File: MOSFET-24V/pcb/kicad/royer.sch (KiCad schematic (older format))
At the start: 26 parts, among them J1 9-24V, J2 COIL, Q1 IRFB4410, Q2 IRFD110, Q3 IRFD110, Q4 IRFB4410

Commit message: compacting PCB
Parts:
- removed C5: 4.7uF, Capacitors_Tantalum_SMD:Tantalum_Case-C_EIA-6032-28_Hand, symbol CP
- added C5: 47nF, Capacitors_SMD:C_1206_HandSoldering, symbol C
- added R6: 1k, Resistors_SMD:R_1206_HandSoldering, symbol R
- R5: renamed from R7; value 1.5k -> 1k
- renumbered R3 to R2, R4 to R3, R5 to R4
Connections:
- net 24V: now also R6.1; no longer R5.1
- net 9V: now also C5.1
- net GND: now also C5.2
- new net: R5.1, R6.2
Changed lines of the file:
@@
 $EndComp
 $Comp
-L R R3
+L R R2
 U 1 1 584180F8
 P 3250 4300
-F 0 "R3" V 3330 4300 50  0000 C CNN
+F 0 "R2" V 3330 4300 50  0000 C CNN
 F 1 "47k" V 3250 4300 50  0000 C CNN
 F 2 "Resistors_SMD:R_1206_HandSoldering" V 3180 4300 50  0001 C CNN
@@
 $EndComp
 $Comp
-L R R5
+L R R4
 U 1 1 58419AC4
 P 3800 4950
-F 0 "R5" V 3880 4950 50  0000 C CNN
+F 0 "R4" V 3880 4950 50  0000 C CNN
 F 1 "33k" V 3800 4950 50  0000 C CNN
 F 2 "Resistors_SMD:R_1206_HandSoldering" V 3730 4950 50  0001 C CNN
@@
 $EndComp
 $Comp
-L R R4
+L R R3
 U 1 1 58419ACA
 P 3550 4300
-F 0 "R4" V 3630 4300 50  0000 C CNN
+F 0 "R3" V 3630 4300 50  0000 C CNN
 F 1 "47k" V 3550 4300 50  0000 C CNN
 F 2 "Resistors_SMD:R_1206_HandSoldering" V 3480 4300 50  0001 C CNN
@@
 Connection ~ 4800 4650
 $Comp
-L R R7
+L R R5
 U 1 1 5841F0FF
 P 5100 4350
-F 0 "R7" V 5180 4350 50  0000 C CNN
-F 1 "1.5k" V 5100 4350 50  0000 C CNN
+F 0 "R5" V 5180 4350 50  0000 C CNN
+F 1 "1k" V 5100 4350 50  0000 C CNN
 F 2 "Resistors_SMD:R_1206_HandSoldering" V 5030 4350 50  0001 C CNN
 F 3 "" H 5100 4350 50  0000 C CNN
@@
 Connection ~ 3800 4100
 Connection ~ 4450 5800
-Wire Wire Line
-	5100 3350 5100 4200
 Wire Wire Line
 	3400 3700 5100 3700
@@
 Connection ~ 2350 3850
 $Comp
-L CP C5
-U 1 1 58F49BFC
+L C C5
+U 1 1 58F49D26
 P 4800 4900
 F 0 "C5" H 4825 5000 50  0000 L CNN
-F 1 "4.7uF" H 4825 4800 50  0000 L CNN
-F 2 "Capacitors_Tantalum_SMD:Tantalum_Case-C_EIA-6032-28_Hand" H 4838 4750 50  0001 C CNN
+F 1 "47nF" H 4825 4800 50  0000 L CNN
+F 2 "Capacitors_SMD:C_1206_HandSoldering" H 4838 4750 50  0001 C CNN
 F 3 "" H 4800 4900 50  0000 C CNN
 	1    4800 4900
 	1    0    0    -1
 $EndComp
+$Comp
+L R R6
+U 1 1 58F4A65C
+P 5100 4050
+F 0 "R6" V 5180 4050 50  0000 C CNN
+F 1 "1k" V 5100 4050 50  0000 C CNN
+F 2 "Resistors_SMD:R_1206_HandSoldering" V 5030 4050 50  0001 C CNN
+F 3 "" H 5100 4050 50  0000 C CNN
+	1    5100 4050
+	1    0    0    -1
+$EndComp
+Wire Wire Line
+	5100 3350 5100 3900
 $EndSCHEMATC

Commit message: enlarging holes 3.2->3.5 mm# Please enter the commit message for your changes. Lines starting
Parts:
- H1, H2, H3, H4: value 3.2mm -> 3.5mm; footprint Mounting_Holes:MountingHole_3.2mm_M3_ISO14580_Pad -> Mounting_Holes:MountingHole_3.5mm_Pad
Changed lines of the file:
@@
 P 3250 6200
 F 0 "H2" H 3250 6300 50  0000 C CNN
-F 1 "3.2mm" V 3350 6200 50  0000 C CNN
-F 2 "Mounting_Holes:MountingHole_3.2mm_M3_ISO14580_Pad" H 3250 6200 50  0001 C CNN
+F 1 "3.5mm" V 3350 6200 50  0000 C CNN
+F 2 "Mounting_Holes:MountingHole_3.5mm_Pad" H 3250 6200 50  0001 C CNN
 F 3 "" H 3250 6200 50  0000 C CNN
 	1    3250 6200
@@
 P 2900 6200
 F 0 "H1" H 2900 6300 50  0000 C CNN
-F 1 "3.2mm" V 3000 6200 50  0000 C CNN
-F 2 "Mounting_Holes:MountingHole_3.2mm_M3_ISO14580_Pad" H 2900 6200 50  0001 C CNN
+F 1 "3.5mm" V 3000 6200 50  0000 C CNN
+F 2 "Mounting_Holes:MountingHole_3.5mm_Pad" H 2900 6200 50  0001 C CNN
 F 3 "" H 2900 6200 50  0000 C CNN
 	1    2900 6200
@@
 P 3900 6200
 F 0 "H4" H 3900 6300 50  0000 C CNN
-F 1 "3.2mm" V 4000 6200 50  0000 C CNN
-F 2 "Mounting_Holes:MountingHole_3.2mm_M3_ISO14580_Pad" H 3900 6200 50  0001 C CNN
+F 1 "3.5mm" V 4000 6200 50  0000 C CNN
+F 2 "Mounting_Holes:MountingHole_3.5mm_Pad" H 3900 6200 50  0001 C CNN
 F 3 "" H 3900 6200 50  0000 C CNN
 	1    3900 6200
@@
 P 3550 6200
 F 0 "H3" H 3550 6300 50  0000 C CNN
-F 1 "3.2mm" V 3650 6200 50  0000 C CNN
-F 2 "Mounting_Holes:MountingHole_3.2mm_M3_ISO14580_Pad" H 3550 6200 50  0001 C CNN
+F 1 "3.5mm" V 3650 6200 50  0000 C CNN
+F 2 "Mounting_Holes:MountingHole_3.5mm_Pad" H 3550 6200 50  0001 C CNN
 F 3 "" H 3550 6200 50  0000 C CNN
 	1    3550 6200

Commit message: footprint for small TO-220 heatsink
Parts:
- Q1, Q4: footprint TO-220:TO-220_Neutral123_Horizontal_LargePads -> TO-220-small-heatsink:TO-220-small-heatsink
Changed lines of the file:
@@
 F 0 "Q1" H 2400 5400 50  0000 R CNN
 F 1 "IRFB4410" V 2700 5500 50  0000 R CNN
-F 2 "TO-220:TO-220_Neutral123_Horizontal_LargePads" H 2650 5400 50  0001 C CNN
+F 2 "TO-220-small-heatsink:TO-220-small-heatsink" H 2650 5400 50  0001 C CNN
 F 3 "" H 2450 5300 50  0000 C CNN
 	1    2450 5300
@@
 F 0 "Q4" H 4300 5400 50  0000 R CNN
 F 1 "IRFB4410" V 4600 5500 50  0000 R CNN
-F 2 "TO-220:TO-220_Neutral123_Horizontal_LargePads" H 4550 5400 50  0001 C CNN
+F 2 "TO-220-small-heatsink:TO-220-small-heatsink" H 4550 5400 50  0001 C CNN
 F 3 "" H 4350 5300 50  0000 C CNN
 	1    4350 5300

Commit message: compacting PCB (using only 4 screw terminals)
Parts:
- removed J1: 9-24V, Connectors_Phoenix:PhoenixContact_MC-G_02x5.08mm_Angled, symbol Screw_Terminal_1x02
- removed J2: COIL, Connectors_Phoenix:PhoenixContact_MC-G_03x5.08mm_Angled, symbol Screw_Terminal_1x03
- added J1: Screw_Terminal_1x04, Connectors_Phoenix:PhoenixContact_MCV-G_04x5.08mm_Vertical, symbol Screw_Terminal_1x04
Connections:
- wire segments 55 -> 52
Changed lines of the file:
@@
 $EndComp
 Wire Wire Line
-	2350 3550 2350 5100
+	2350 3850 2350 5100
 Wire Wire Line
 	2350 4500 2400 4500
@@
 	2350 5500 2350 5800
 Wire Wire Line
-	2350 5800 4800 5800
+	4800 5800 2350 5800
 Connection ~ 2750 5800
 Connection ~ 2750 5150
@@
 	3250 4500 3550 5300
 Wire Wire Line
-	4450 3550 4450 5100
+	4450 3850 4450 5100
 Wire Wire Line
 	4450 4500 4400 4500
@@
 Connection ~ 3800 4100
 Connection ~ 4450 5800
-Wire Wire Line
-	3400 3700 5100 3700
 Connection ~ 5100 4650
-Connection ~ 5100 3700
-$Comp
-L GND #PWR01
+$Comp
+L GND #PWR5
 U 1 1 5842503E
 P 4800 6000
-F 0 "#PWR01" H 4800 5750 50  0001 C CNN
+F 0 "#PWR5" H 4800 5750 50  0001 C CNN
 F 1 "GND" H 4800 5850 50  0000 C CNN
 F 2 "" H 4800 6000 50  0000 C CNN
@@
 	1    4250 4500
 	-1   0    0    -1
-$EndComp
-$Comp
-L Screw_Terminal_1x03 J2
-U 1 1 58F34C5A
-P 3400 3150
-F 0 "J2" H 3400 3500 50  0000 C TNN
-F 1 "COIL" V 3250 3150 50  0000 C TNN
-F 2 "Connectors_Phoenix:PhoenixContact_MC-G_03x5.08mm_Angled" H 3400 2825 50  0001 C CNN
-F 3 "" H 3375 3250 50  0001 C CNN
-	1    3400 3150
-	0    -1   1    0
-$EndComp
-Wire Wire Line
-	2350 3550 3200 3550
-Wire Wire Line
-	3200 3550 3200 3350
-Wire Wire Line
-	3600 3350 3600 3550
-Wire Wire Line
-	3600 3550 4450 3550
-Wire Wire Line
-	3400 3350 3400 3700
-$Comp
-L Screw_Terminal_1x02 J1
-U 1 1 58F35B2E
-P 5200 3150
-F 0 "J1" H 5200 3400 50  0000 C TNN
-F 1 "9-24V" V 5050 3150 50  0000 C TNN
-F 2 "Connectors_Phoenix:PhoenixContact_MC-G_02x5.08mm_Angled" H 5200 2925 50  0001 C CNN
-F 3 "" H 5175 3150 50  0001 C CNN
-	1    5200 3150
-	0    -1   1    0
 $EndComp
 Text Label 2350 5050 0    60   ~ 0
@@
 Text Label 4050 4100 0    60   ~ 0
 9V
-Text Label 4750 3700 0    60   ~ 0
+Text Label 5100 3800 0    60   ~ 0
 24V
 $Comp
-L GND #PWR02
+L GND #PWR6
 U 1 1 58F35A7F
-P 5300 3350
-F 0 "#PWR02" H 5300 3100 50  0001 C CNN
-F 1 "GND" H 5300 3200 50  0000 C CNN
-F 2 "" H 5300 3350 50  0000 C CNN
-F 3 "" H 5300 3350 50  0000 C CNN
-	1    5300 3350
-	1    0    0    -1
+P 6700 4500
+F 0 "#PWR6" H 6700 4250 50  0001 C CNN
+F 1 "GND" H 6700 4350 50  0000 C CNN
+F 2 "" H 6700 4500 50  0000 C CNN
+F 3 "" H 6700 4500 50  0000 C CNN
+	1    6700 4500
+	0    -1   -1   0
 $EndComp
 $Comp
@@
 $EndComp
 $Comp
-L GND #PWR03
+L GND #PWR1
 U 1 1 58F46F6F
 P 2900 6400
-F 0 "#PWR03" H 2900 6150 50  0001 C CNN
+F 0 "#PWR1" H 2900 6150 50  0001 C CNN
 F 1 "GND" H 2900 6250 50  0000 C CNN
 F 2 "" H 2900 6400 50  0000 C CNN
@@
 $EndComp
 $Comp
-L GND #PWR04
+L GND #PWR2
 U 1 1 58F47000
 P 3250 6400
-F 0 "#PWR04" H 3250 6150 50  0001 C CNN
+F 0 "#PWR2" H 3250 6150 50  0001 C CNN
 F 1 "GND" H 3250 6250 50  0000 C CNN
 F 2 "" H 3250 6400 50  0000 C CNN
@@
 $EndComp
 $Comp
-L GND #PWR05
+L GND #PWR3
 U 1 1 58F47046
 P 3550 6400
-F 0 "#PWR05" H 3550 6150 50  0001 C CNN
+F 0 "#PWR3" H 3550 6150 50  0001 C CNN
 F 1 "GND" H 3550 6250 50  0000 C CNN
 F 2 "" H 3550 6400 50  0000 C CNN
@@
 $EndComp
 $Comp
-L GND #PWR06
+L GND #PWR4
 U 1 1 58F470A5
 P 3900 6400
-F 0 "#PWR06" H 3900 6150 50  0001 C CNN
+F 0 "#PWR4" H 3900 6150 50  0001 C CNN
 F 1 "GND" H 3900 6250 50  0000 C CNN
 F 2 "" H 3900 6400 50  0000 C CNN
@@
 Wire Wire Line
 	3550 3850 4450 3850
-Connection ~ 4450 3850
 Wire Wire Line
 	3250 3850 2350 3850
-Connection ~ 2350 3850
 $Comp
 L C C5
@@
 $EndComp
 Wire Wire Line
-	5100 3350 5100 3900
+	5100 3700 5100 3900
+$Comp
+L Screw_Terminal_1x04 J1
+U 1 1 58FB71E3
+P 6500 4400
+F 0 "J1" H 6500 4850 50  0000 C TNN
+F 1 "Screw_Terminal_1x04" V 6350 4400 50  0000 C TNN
+F 2 "Connectors_Phoenix:PhoenixContact_MCV-G_04x5.08mm_Vertical" H 6500 3975 50  0001 C CNN
+F 3 "" H 6475 4600 50  0001 C CNN
+	1    6500 4400
+	1    0    0    -1
+$EndComp
+Wire Wire Line
+	6700 4300 6950 4300
+Text Label 6750 4300 0    60   ~ 0
+24V
+Wire Wire Line
+	6700 4100 6950 4100
+Wire Wire Line
+	6700 4700 6950 4700
+Text Label 6750 4100 0    60   ~ 0
+C1
+Text Label 6750 4700 0    60   ~ 0
+C2
 $EndSCHEMATC

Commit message: increasing drill hole sizes in to-220 and screw terminal footprints
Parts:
- J1: footprint Connectors_Phoenix:PhoenixContact_MCV-G_04x5.08mm_Vertical -> screw-4-pin:screw-terminal-4-pin
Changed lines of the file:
@@
 	2350 5500 2350 5800
 Wire Wire Line
-	4800 5800 2350 5800
+	2350 5800 4800 5800
 Connection ~ 2750 5800
 Connection ~ 2750 5150
@@
 Connection ~ 5100 4650
 $Comp
-L GND #PWR5
+L GND #PWR01
 U 1 1 5842503E
 P 4800 6000
-F 0 "#PWR5" H 4800 5750 50  0001 C CNN
+F 0 "#PWR01" H 4800 5750 50  0001 C CNN
 F 1 "GND" H 4800 5850 50  0000 C CNN
 F 2 "" H 4800 6000 50  0000 C CNN
@@
 24V
 $Comp
-L GND #PWR6
+L GND #PWR02
 U 1 1 58F35A7F
 P 6700 4500
-F 0 "#PWR6" H 6700 4250 50  0001 C CNN
+F 0 "#PWR02" H 6700 4250 50  0001 C CNN
 F 1 "GND" H 6700 4350 50  0000 C CNN
 F 2 "" H 6700 4500 50  0000 C CNN
@@
 $EndComp
 $Comp
-L GND #PWR1
+L GND #PWR03
 U 1 1 58F46F6F
 P 2900 6400
-F 0 "#PWR1" H 2900 6150 50  0001 C CNN
+F 0 "#PWR03" H 2900 6150 50  0001 C CNN
 F 1 "GND" H 2900 6250 50  0000 C CNN
 F 2 "" H 2900 6400 50  0000 C CNN
@@
 $EndComp
 $Comp
-L GND #PWR2
+L GND #PWR04
 U 1 1 58F47000
 P 3250 6400
-F 0 "#PWR2" H 3250 6150 50  0001 C CNN
+F 0 "#PWR04" H 3250 6150 50  0001 C CNN
 F 1 "GND" H 3250 6250 50  0000 C CNN
 F 2 "" H 3250 6400 50  0000 C CNN
@@
 $EndComp
 $Comp
-L GND #PWR3
+L GND #PWR05
 U 1 1 58F47046
 P 3550 6400
-F 0 "#PWR3" H 3550 6150 50  0001 C CNN
+F 0 "#PWR05" H 3550 6150 50  0001 C CNN
 F 1 "GND" H 3550 6250 50  0000 C CNN
 F 2 "" H 3550 6400 50  0000 C CNN
@@
 $EndComp
 $Comp
-L GND #PWR4
+L GND #PWR06
 U 1 1 58F470A5
 P 3900 6400
-F 0 "#PWR4" H 3900 6150 50  0001 C CNN
+F 0 "#PWR06" H 3900 6150 50  0001 C CNN
 F 1 "GND" H 3900 6250 50  0000 C CNN
 F 2 "" H 3900 6400 50  0000 C CNN
@@
 F 0 "J1" H 6500 4850 50  0000 C TNN
 F 1 "Screw_Terminal_1x04" V 6350 4400 50  0000 C TNN
-F 2 "Connectors_Phoenix:PhoenixContact_MCV-G_04x5.08mm_Vertical" H 6500 3975 50  0001 C CNN
+F 2 "screw-4-pin:screw-terminal-4-pin" H 6500 3975 50  0001 C CNN
 F 3 "" H 6475 4600 50  0001 C CNN
 	1    6500 4400

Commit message: changing values on MOSFET circuit
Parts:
- C1, C2, C3, C4: value 47nF -> 10nF
- C5: value 47nF -> 470nF
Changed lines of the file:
@@
 P 2550 4750
 F 0 "C1" H 2575 4850 50  0000 L CNN
-F 1 "47nF" H 2575 4650 50  0000 L CNN
+F 1 "10nF" H 2575 4650 50  0000 L CNN
 F 2 "Capacitors_SMD:C_1206_HandSoldering" H 2588 4600 50  0001 C CNN
 F 3 "" H 2550 4750 50  0000 C CNN
@@
 P 2750 4950
 F 0 "C2" H 2775 5050 50  0000 L CNN
-F 1 "47nF" H 2550 4850 50  0000 L CNN
+F 1 "10nF" H 2550 4850 50  0000 L CNN
 F 2 "Capacitors_SMD:C_1206_HandSoldering" H 2788 4800 50  0001 C CNN
 F 3 "" H 2750 4950 50  0000 C CNN
@@
 P 4250 4750
 F 0 "C4" H 4275 4850 50  0000 L CNN
-F 1 "47nF" H 4275 4650 50  0000 L CNN
+F 1 "10nF" H 4275 4650 50  0000 L CNN
 F 2 "Capacitors_SMD:C_1206_HandSoldering" H 4288 4600 50  0001 C CNN
 F 3 "" H 4250 4750 50  0000 C CNN
@@
 P 4050 4950
 F 0 "C3" H 4075 5050 50  0000 L CNN
-F 1 "47nF" H 3850 4850 50  0000 L CNN
+F 1 "10nF" H 3850 4850 50  0000 L CNN
 F 2 "Capacitors_SMD:C_1206_HandSoldering" H 4088 4800 50  0001 C CNN
 F 3 "" H 4050 4950 50  0000 C CNN
@@
 P 4800 4900
 F 0 "C5" H 4825 5000 50  0000 L CNN
-F 1 "47nF" H 4825 4800 50  0000 L CNN
+F 1 "470nF" H 4825 4800 50  0000 L CNN
 F 2 "Capacitors_SMD:C_1206_HandSoldering" H 4838 4750 50  0001 C CNN
 F 3 "" H 4800 4900 50  0000 C CNN

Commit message: Change from 10nF/10nF to 22nF/10nF capacitive divider
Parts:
- C1, C4: value 10nF -> 22nF
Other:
- note added: "C1=C2=C3=C4=10nF works.\nTry C1=C4=22nF C2=C3=10nF\nfor faster switching, less heating"
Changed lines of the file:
@@
 P 2550 4750
 F 0 "C1" H 2575 4850 50  0000 L CNN
-F 1 "10nF" H 2575 4650 50  0000 L CNN
+F 1 "22nF" H 2575 4650 50  0000 L CNN
 F 2 "Capacitors_SMD:C_1206_HandSoldering" H 2588 4600 50  0001 C CNN
 F 3 "" H 2550 4750 50  0000 C CNN
@@
 P 4250 4750
 F 0 "C4" H 4275 4850 50  0000 L CNN
-F 1 "10nF" H 4275 4650 50  0000 L CNN
+F 1 "22nF" H 4275 4650 50  0000 L CNN
 F 2 "Capacitors_SMD:C_1206_HandSoldering" H 4288 4600 50  0001 C CNN
 F 3 "" H 4250 4750 50  0000 C CNN
@@
 Text Label 6750 4700 0    60   ~ 0
 C2
+Text Notes 2650 6950 0    60   ~ 0
+C1=C2=C3=C4=10nF works.\nTry C1=C4=22nF C2=C3=10nF\nfor faster switching, less heating
 $EndSCHEMATC

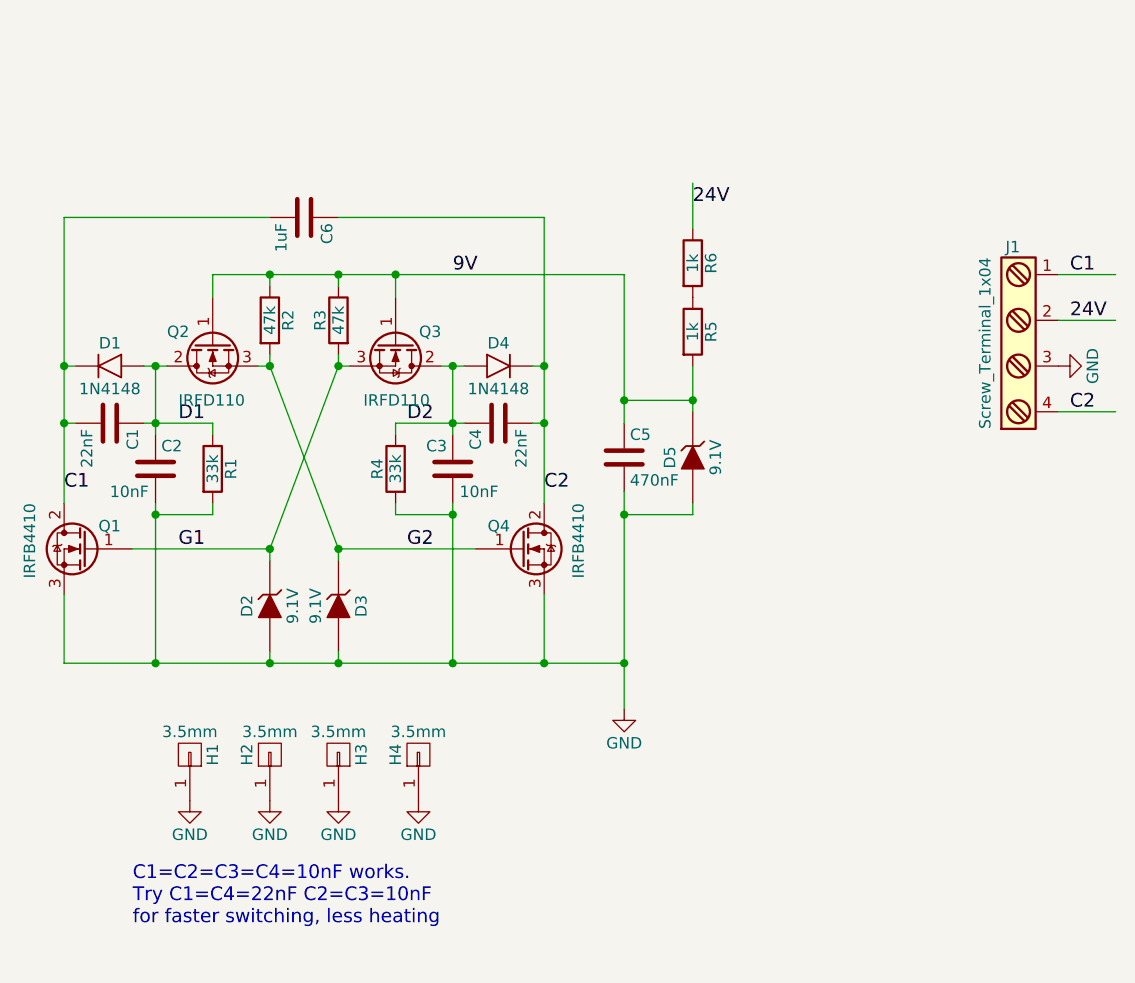
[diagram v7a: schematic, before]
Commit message: revert back to 10nF
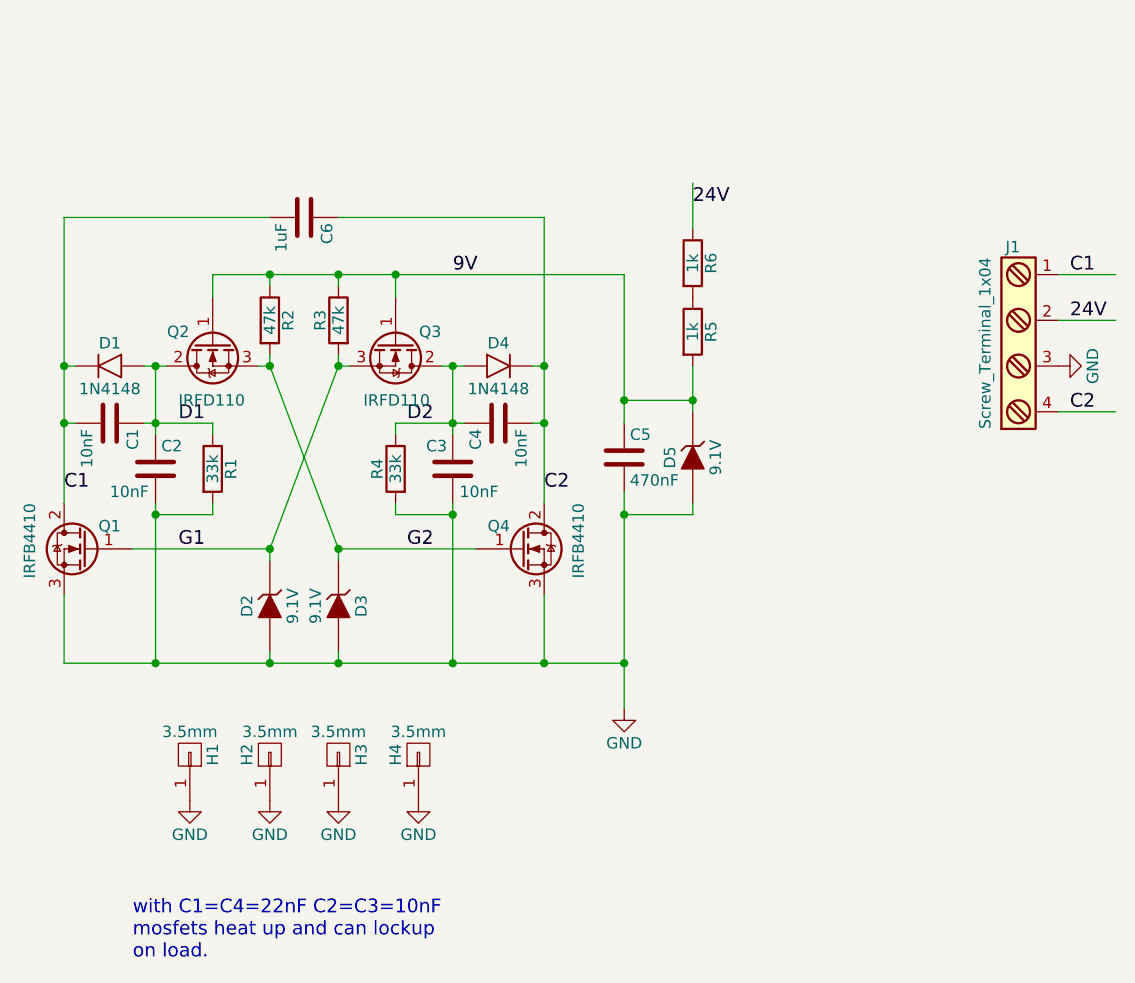
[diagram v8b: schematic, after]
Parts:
- C1, C4: value 22nF -> 10nF
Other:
- note added: "with C1=C4=22nF C2=C3=10nF\nmosfets heat up and can lockup\non load."
- note removed: "C1=C2=C3=C4=10nF works.\nTry C1=C4=22nF C2=C3=10nF\nfor faster switching, less heating"
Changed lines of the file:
@@
 P 2550 4750
 F 0 "C1" H 2575 4850 50  0000 L CNN
-F 1 "22nF" H 2575 4650 50  0000 L CNN
+F 1 "10nF" H 2575 4650 50  0000 L CNN
 F 2 "Capacitors_SMD:C_1206_HandSoldering" H 2588 4600 50  0001 C CNN
 F 3 "" H 2550 4750 50  0000 C CNN
@@
 P 4250 4750
 F 0 "C4" H 4275 4850 50  0000 L CNN
-F 1 "22nF" H 4275 4650 50  0000 L CNN
+F 1 "10nF" H 4275 4650 50  0000 L CNN
 F 2 "Capacitors_SMD:C_1206_HandSoldering" H 4288 4600 50  0001 C CNN
 F 3 "" H 4250 4750 50  0000 C CNN
@@
 Text Label 6750 4700 0    60   ~ 0
 C2
-Text Notes 2650 6950 0    60   ~ 0
-C1=C2=C3=C4=10nF works.\nTry C1=C4=22nF C2=C3=10nF\nfor faster switching, less heating
+Text Notes 2650 7100 0    60   ~ 0
+with C1=C4=22nF C2=C3=10nF\nmosfets heat up and can lockup\non load.
 $EndSCHEMATC
